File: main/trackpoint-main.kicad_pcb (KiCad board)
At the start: 2 copper layers, 27.5 x 35 mm, 28 parts, among them P1 CONN_10, P2 CONN_5, P3 CONN_8, SW1 CMI126603D08, SW2 CMI126603D08, U1 MKL03Z32VFK4, U4 ESD

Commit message: Capitalize UGL library name for the board.
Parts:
- removed the ? at (194.2, 126.5)
- removed the ? at (213.8, 139.5)
- removed the ? at (194.2, 139.5)
- removed the ? at (210.8, 135.1)
- removed the ? at (210.8, 125.6)
- removed the ? at (201.3, 135.1)
- removed the ? at (201.3, 125.6)
- added ?: , UGL:hole_2.8mm, F.Cu at (194.2, 126.5)
- added ?: , UGL:hole_2.8mm, F.Cu at (213.8, 139.5)
- added ?: , UGL:hole_2.8mm, F.Cu at (194.2, 139.5)
- added ?: , UGL:hole_2.5mm, F.Cu at (210.8, 135.1)
- added ?: , UGL:hole_2.5mm, F.Cu at (210.8, 125.6)
- added ?: , UGL:hole_2.5mm, F.Cu at (201.3, 135.1)
- added ?: , UGL:hole_2.5mm, F.Cu at (201.3, 125.6)
- C12, C2, C3, C4, C7, C8, FB2, R1, R2, R6, R7: footprint ugl:SM0603 -> UGL:SM0603
- D2: footprint ugl:SM0603_Diode -> UGL:SM0603_Diode
- G***: footprint ugl:UHK_Logo_12x3.4_mm -> UGL:UHK_Logo_12x3.4_mm
- P1: footprint ugl:Tag_Connect_2x5_Header_With_No_Legs_Parallel_Numbering -> UGL:Tag_Connect_2x5_Header_With_No_Legs_Parallel_Numbering
- P2: footprint ugl:UHK_Male_Pogo_Pin_v2 -> UGL:UHK_Male_Pogo_Pin_v2
- P3: footprint ugl:84981-8 -> UGL:84981-8
- SW1, SW2: footprint ugl:CMI126603D08 -> UGL:CMI126603D08
- U1: footprint ugl:QFN-24-1EP_4x4mm_Pitch0.5mm -> UGL:QFN-24-1EP_4x4mm_Pitch0.5mm
- U4: footprint ugl:SC-74-TVS -> UGL:SC-74-TVS
- VR1: footprint ugl:SOT-23-5 -> UGL:SOT-23-5
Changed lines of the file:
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@@
     (add_net "Net-(VR1-Pad4)")
   )
-  (module ugl:QFN-24-1EP_4x4mm_Pitch0.5mm (layer F.Cu)
+  (module UGL:QFN-24-1EP_4x4mm_Pitch0.5mm (layer F.Cu)
     (at 204.5 130.6 180)
     (descr "24-Lead Plastic Quad Flat, No Lead Package (MJ) - 4x4x0.9 mm Body [QFN]; (see Microchip Packaging Specification 00000049BS.pdf)")
@@
     )
   )
-  (module ugl:hole_2.8mm locked (layer F.Cu)
+  (module UGL:hole_2.8mm locked (layer F.Cu)
     (at 194.25 126.5)
     (attr virtual)
@@
     (pad "" np_thru_hole circle (at 0 0) (size 2.8 2.8) (drill 2.8) (layers *.Cu *.Mask))
   )
-  (module ugl:hole_2.8mm locked (layer F.Cu)
+  (module UGL:hole_2.8mm locked (layer F.Cu)
     (at 213.75 139.5)
     (attr virtual)
@@
     (pad "" np_thru_hole circle (at 0 0) (size 2.8 2.8) (drill 2.8) (layers *.Cu *.Mask))
   )
-  (module ugl:hole_2.8mm locked (layer F.Cu)
+  (module UGL:hole_2.8mm locked (layer F.Cu)
     (at 194.25 139.5)
     (attr virtual)
@@
     (pad "" np_thru_hole circle (at 0 0) (size 2.8 2.8) (drill 2.8) (layers *.Cu *.Mask))
   )
-  (module ugl:CMI126603D08 locked (layer F.Cu)
+  (module UGL:CMI126603D08 locked (layer F.Cu)
     (at 212.660004 144.268997 180)
     (fp_text reference SW2 (at -3.839996 3.468997) (layer F.SilkS)
@@
       (net 36 /SW2))
   )
-  (module ugl:CMI126603D08 locked (layer F.Cu)
+  (module UGL:CMI126603D08 locked (layer F.Cu)
     (at 199.360001 144.268997)
     (fp_text reference SW1 (at 0.039999 -3.668997) (layer F.SilkS)
@@
       (net 35 /SW1))
   )
-  (module ugl:SM0603_Diode (layer F.Cu)
+  (module UGL:SM0603_Diode (layer F.Cu)
     (at 206.5 126.2 90)
     (attr virtual)
@@
     )
   )
-  (module ugl:Tag_Connect_2x5_Header_With_No_Legs_Parallel_Numbering (layer F.Cu)
+  (module UGL:Tag_Connect_2x5_Header_With_No_Legs_Parallel_Numbering (layer F.Cu)
     (at 194.3 133.1 90)
     (tags "Tag-Connect TC2050")
@@
     (pad "" np_thru_hole circle (at 3.95 1.016 90) (size 0.98552 0.98552) (drill 0.98552) (layers *.Cu *.Mask))
   )
-  (module ugl:hole_2.5mm locked (layer F.Cu)
+  (module UGL:hole_2.5mm locked (layer F.Cu)
     (at 210.760002 135.119003)
     (attr virtual)
@@
     (pad "" np_thru_hole circle (at 0 0) (size 2.5 2.5) (drill 2.5) (layers *.Cu *.Mask))
   )
-  (module ugl:hole_2.5mm locked (layer F.Cu)
+  (module UGL:hole_2.5mm locked (layer F.Cu)
     (at 210.760002 125.619003)
     (attr virtual)
@@
     (pad "" np_thru_hole circle (at 0 0) (size 2.5 2.5) (drill 2.5) (layers *.Cu *.Mask))
   )
-  (module ugl:hole_2.5mm locked (layer F.Cu)
+  (module UGL:hole_2.5mm locked (layer F.Cu)
     (at 201.260002 135.119003)
     (attr virtual)
@@
     (pad "" np_thru_hole circle (at 0 0) (size 2.5 2.5) (drill 2.5) (layers *.Cu *.Mask))
   )
-  (module ugl:hole_2.5mm locked (layer F.Cu)
+  (module UGL:hole_2.5mm locked (layer F.Cu)
     (at 201.260002 125.619003)
     (attr virtual)
@@
     (pad "" np_thru_hole circle (at 0 0) (size 2.5 2.5) (drill 2.5) (layers *.Cu *.Mask))
   )
-  (module ugl:UHK_Logo_12x3.4_mm (layer B.Cu)
+  (module UGL:UHK_Logo_12x3.4_mm (layer B.Cu)
     (at 198.6 114.6 180)
     (attr virtual)
@@
       (xy 2.621935 -1.146433)) (layer B.Mask) (width 0.01))
   )
-  (module ugl:SC-74-TVS (layer F.Cu)
+  (module UGL:SC-74-TVS (layer F.Cu)
     (at 213.9 128.4 180)
     (attr smd)
@@
     (pad "" smd rect (at 0 -1.2 180) (size 0.6 1) (layers F.Cu F.Paste F.Mask))
   )
-  (module ugl:SM0603 (layer F.Cu)
+  (module UGL:SM0603 (layer F.Cu)
     (at 207.8 130.6 270)
     (attr smd)
@@
     )
   )
-  (module ugl:SM0603 (layer F.Cu)
+  (module UGL:SM0603 (layer F.Cu)
     (at 213.9 125.5)
     (attr smd)
@@
     )
   )
-  (module ugl:SM0603 (layer F.Cu)
+  (module UGL:SM0603 (layer F.Cu)
     (at 205.2 138.65 90)
     (attr smd)
@@
     )
   )
-  (module ugl:SM0603 (layer F.Cu)
+  (module UGL:SM0603 (layer F.Cu)
     (at 212.3 132 270)
     (attr smd)
@@
     )
   )
-  (module ugl:SM0603 (layer F.Cu)
+  (module UGL:SM0603 (layer F.Cu)
     (at 205.2 135.6 90)
     (attr smd)
@@
     )
   )
-  (module ugl:SM0603 (layer F.Cu)
+  (module UGL:SM0603 (layer F.Cu)
     (at 205 126.2 270)
     (attr virtual)
@@
     )
   )
-  (module ugl:SM0603 (layer F.Cu)
+  (module UGL:SM0603 (layer F.Cu)
     (at 214.9 132 90)
     (attr smd)
@@
     )
   )
-  (module ugl:SM0603 (layer F.Cu)
+  (module UGL:SM0603 (layer F.Cu)
     (at 213.6 132 90)
     (attr smd)
@@
     )
   )
-  (module ugl:SM0603 (layer F.Cu)
+  (module UGL:SM0603 (layer F.Cu)
     (at 210 139.7 270)
     (attr smd)
@@
     )
   )
-  (module ugl:SM0603 (layer F.Cu)
+  (module UGL:SM0603 (layer F.Cu)
     (at 214.3 136.2 180)
     (attr smd)
@@
     )
   )
-  (module ugl:SM0603 (layer F.Cu)
+  (module UGL:SM0603 (layer F.Cu)
     (at 206.7 135.6 90)
     (attr smd)
@@
     )
   )
-  (module ugl:SOT-23-5 (layer F.Cu)
+  (module UGL:SOT-23-5 (layer F.Cu)
     (at 207.6 139.2 180)
     (tags SOT23)
@@
     )
   )
-  (module ugl:84981-8 locked (layer F.Cu)
+  (module UGL:84981-8 locked (layer F.Cu)
     (at 194.199997 118.468994 270)
     (descr "FFC connector")
@@
       (net 21 /CLK))
   )
-  (module ugl:UHK_Male_Pogo_Pin_v2 locked (layer F.Cu)
+  (module UGL:UHK_Male_Pogo_Pin_v2 locked (layer F.Cu)
     (at 219.75 132.800003)
     (fp_text reference P2 (at -1.15 -8.700003) (layer F.SilkS)

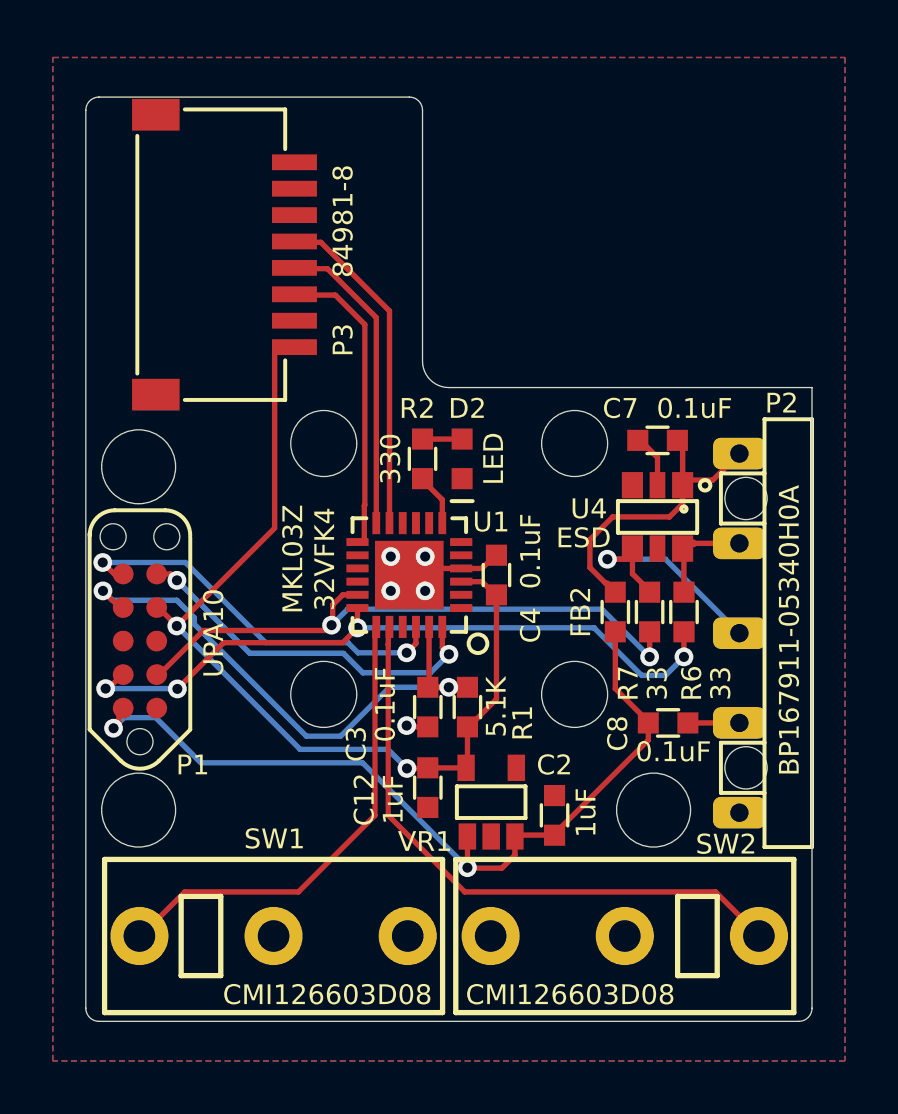
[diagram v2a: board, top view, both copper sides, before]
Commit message: Replace 8 pin, 1 mm pitch connector with 5 pin, 0.5 mm pitch connector.
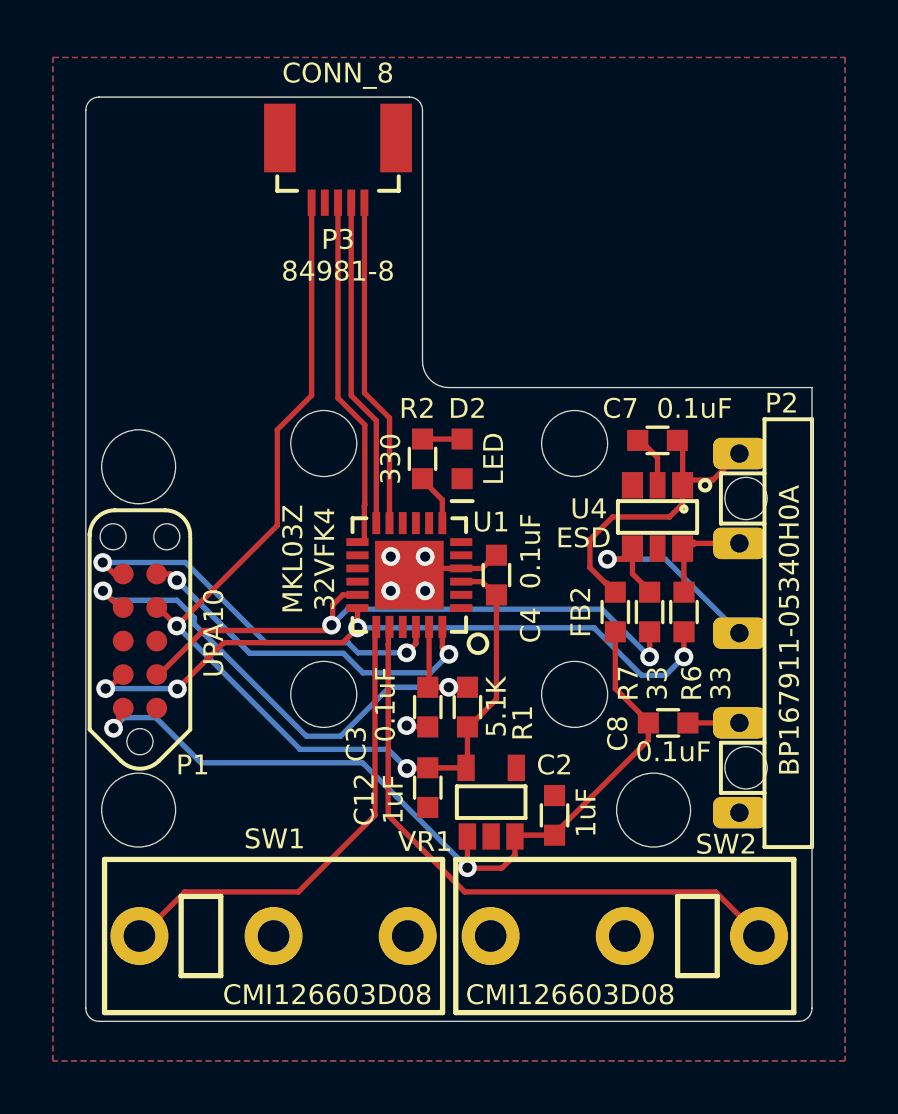
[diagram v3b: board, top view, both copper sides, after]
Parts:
- P3: footprint UGL:84981-8 -> UGL:FFC_Connector_51281-0594
- moved P3 9.66 mm to (201.8, 112.5), turned to 180 degrees
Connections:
- P3 pad 1: Net-(P3-Pad1) -> /DATA
- P3 pad 2: Net-(P3-Pad2) -> /CLK
- P3 pad 3: Net-(P3-Pad3) -> /TP_RST
- P3 pad 4: /DATA -> GND
- P3 pad 5: /CLK -> +3V3
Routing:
- net +3V3: track 33.7 -> 39.6 mm
- net /TP_RST: track 11.3 -> 13.1 mm
- net /CLK: track 11.1 -> 12.2 mm

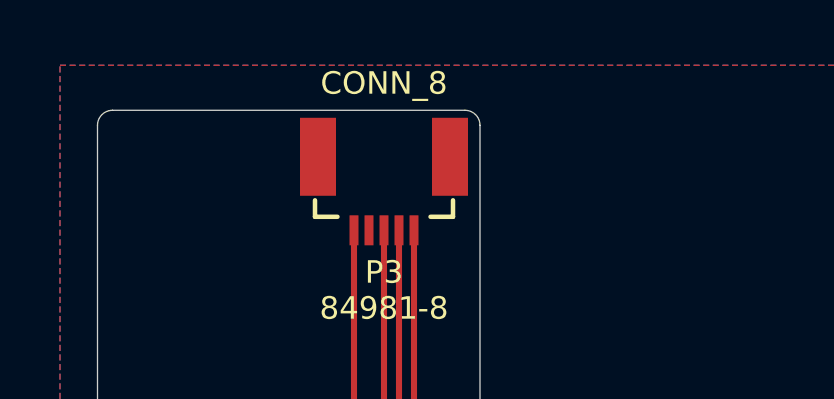
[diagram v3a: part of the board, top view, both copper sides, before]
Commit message: Make the CONN_8 silk screen text invisible.
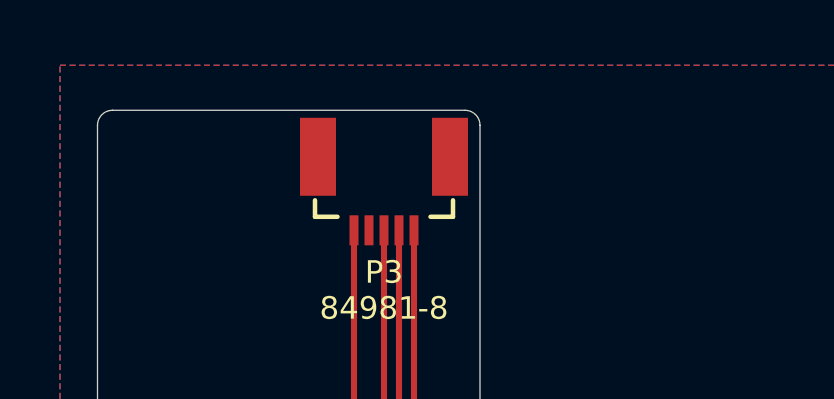
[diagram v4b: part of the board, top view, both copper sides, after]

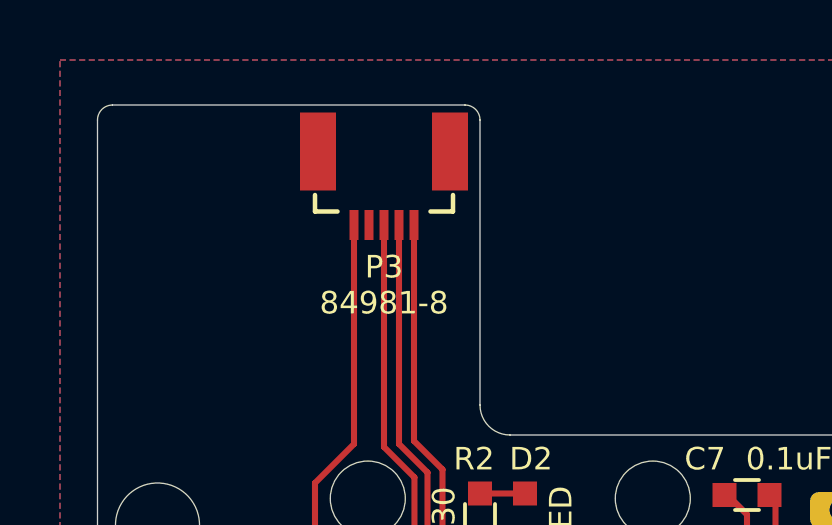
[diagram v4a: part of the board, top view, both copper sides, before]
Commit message: Connect GND all the way.
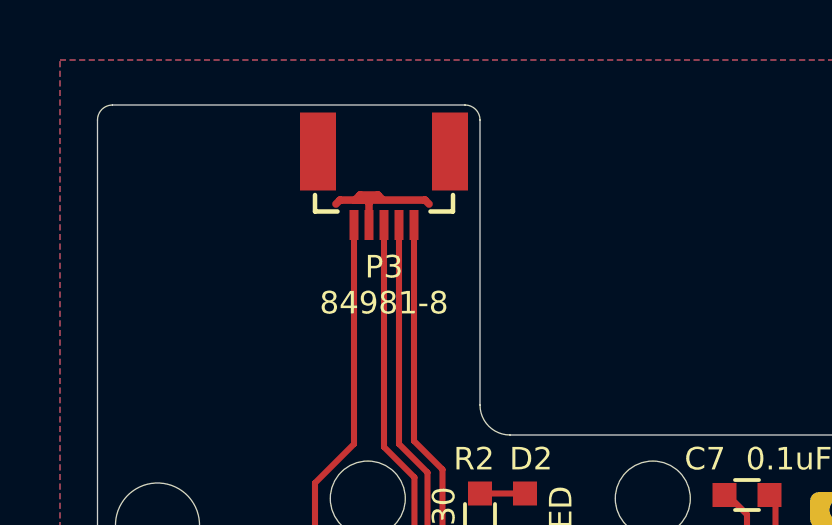
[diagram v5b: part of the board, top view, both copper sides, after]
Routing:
- net GND: track 7.14 -> 12.4 mm

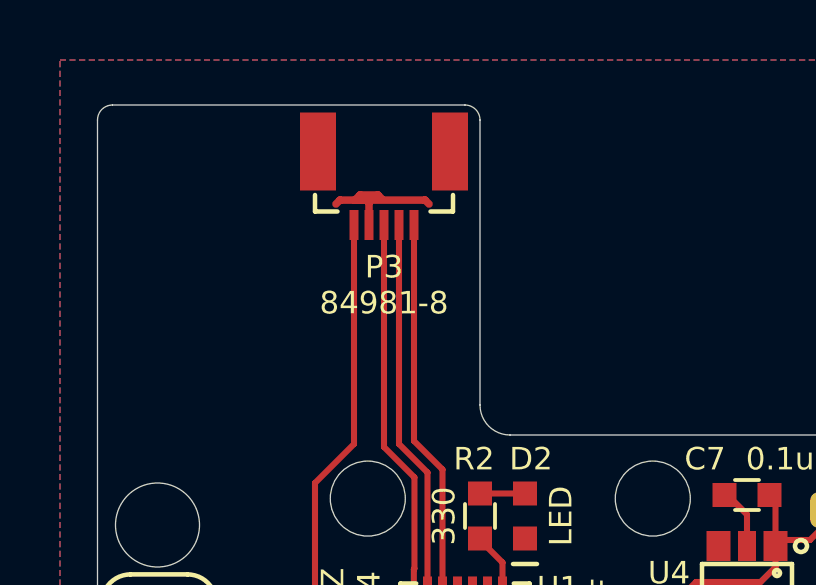
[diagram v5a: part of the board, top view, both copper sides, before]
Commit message: Update FFC connector part number.
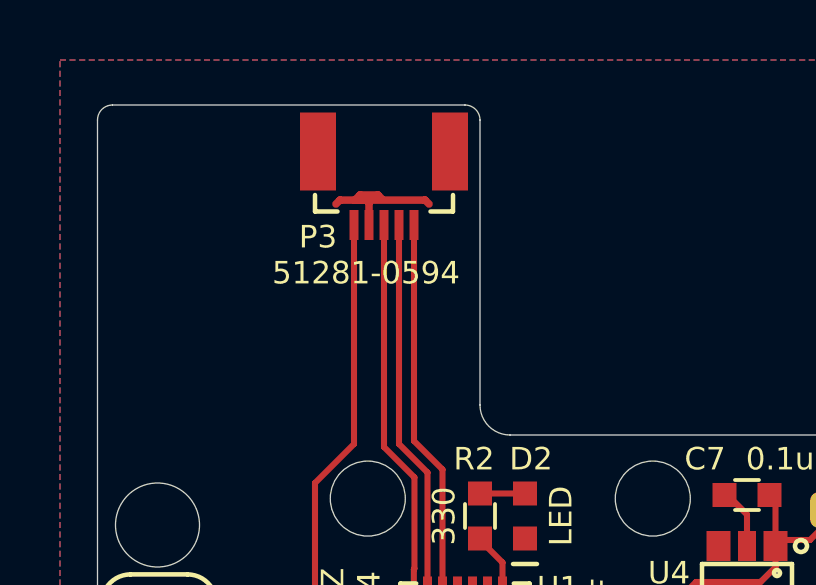
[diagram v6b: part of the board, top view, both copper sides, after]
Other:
- board text added: "51281-0594"
- board text removed: "84981-8"

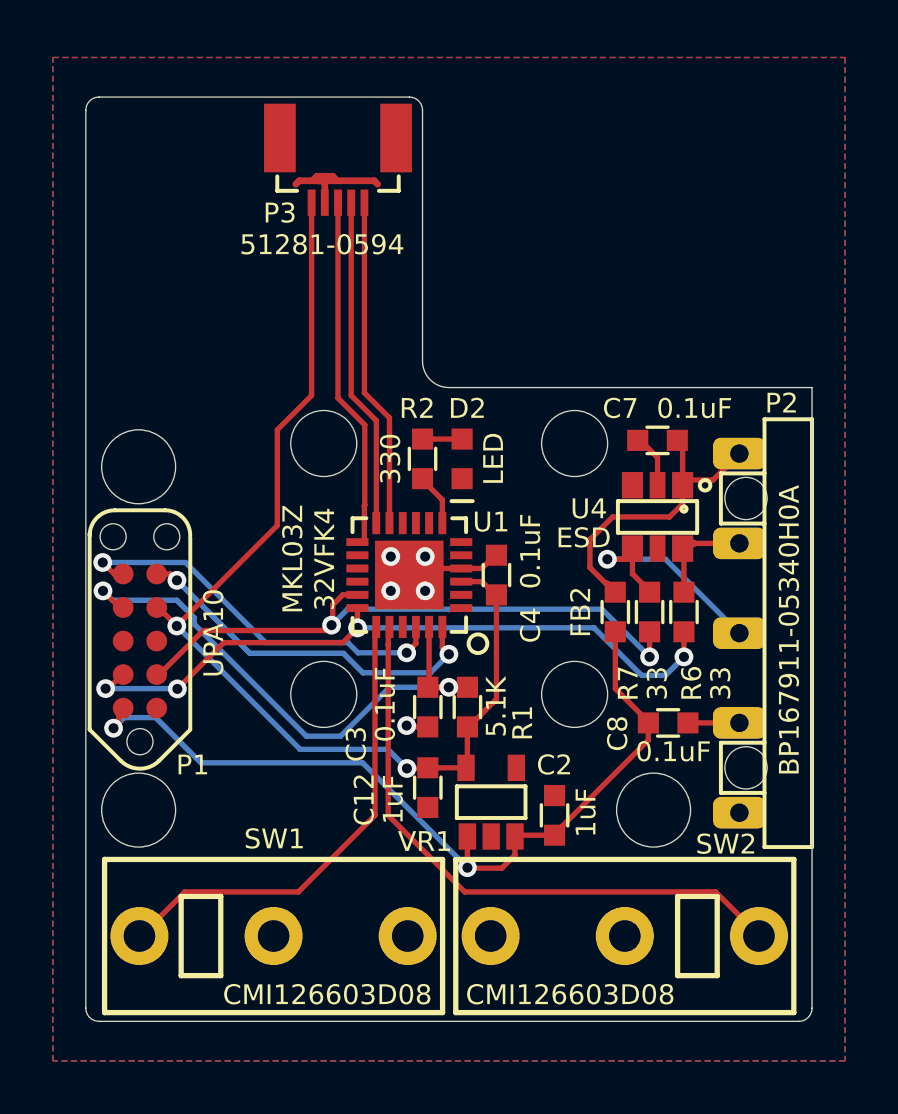
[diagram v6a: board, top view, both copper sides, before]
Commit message: Update FFC connector pinout.
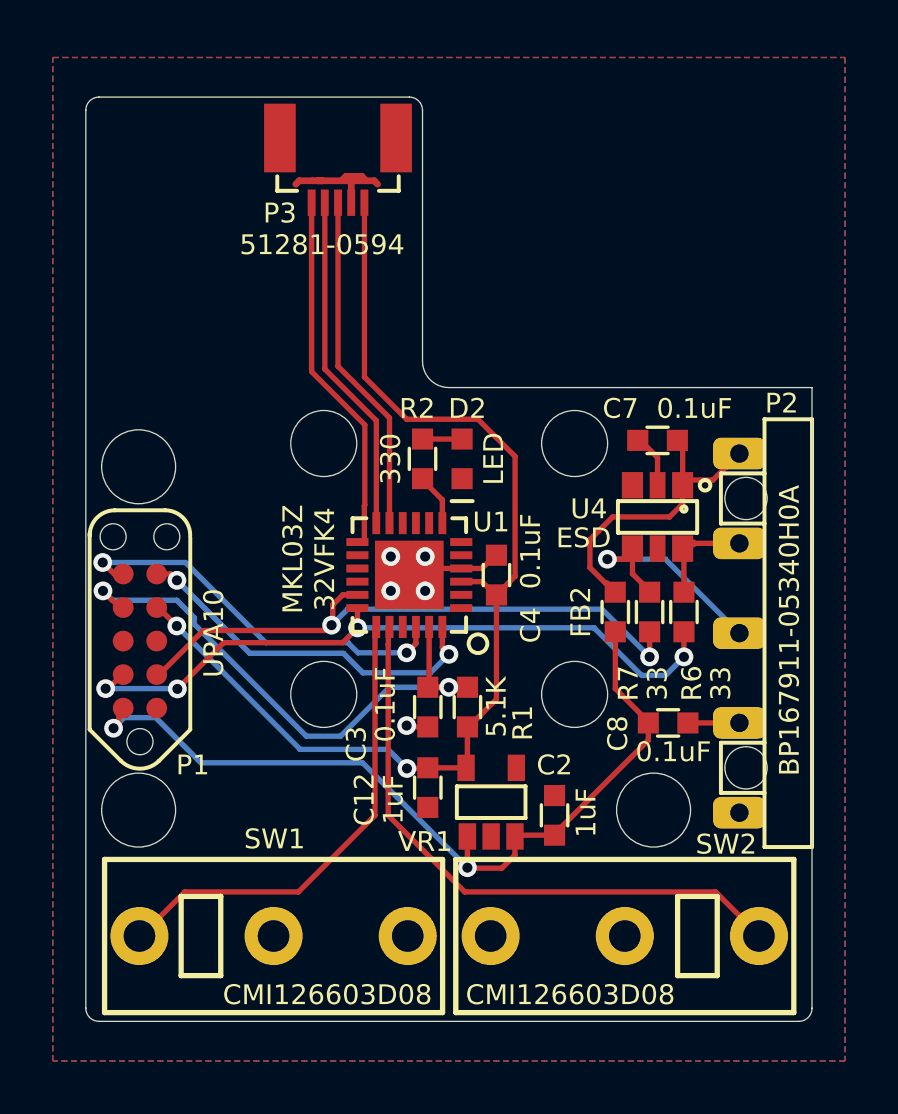
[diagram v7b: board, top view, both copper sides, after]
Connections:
- P3 pad 1: /DATA -> +3V3
- P3 pad 2: /CLK -> GND
- P3 pad 4: GND -> /CLK
- P3 pad 5: +3V3 -> /DATA
- U1 pad 11: /DATA -> /TP_RST
- U1 pad 13: /TP_RST -> /DATA
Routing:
- net /DATA: track 12.1 -> 13.8 mm
- net +3V3: track 39.6 -> 40.9 mm
- net /CLK: track 12.2 -> 12.9 mm

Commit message: Bump main board version to 2.0.0
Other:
- board text added: "PCB ID: trackpoint_main_2.0.0"
- board text removed: "PCB ID: trackpoint_main_1.2.0"
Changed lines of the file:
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@@
   (title_block
     (title "UHK Trackpoint Module")
-    (rev 1.2.0)
+    (rev 2.0.0)
     (company "Ultimate Gadget Laboratories Kft.")
   )
@@
     (effects (font (size 0.75 0.75) (thickness 0.15)))
   )
-  (gr_text "PCB ID: trackpoint_main_1.2.0" (at 206.1 146.5) (layer B.SilkS)
+  (gr_text "PCB ID: trackpoint_main_2.0.0" (at 206.1 146.5) (layer B.SilkS)
     (effects (font (size 0.75 0.75) (thickness 0.15)) (justify mirror))
   )
